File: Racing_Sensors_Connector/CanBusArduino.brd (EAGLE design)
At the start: 48.3 x 40.6 mm, 21 parts, among them U1 328P, Y1 16MHz

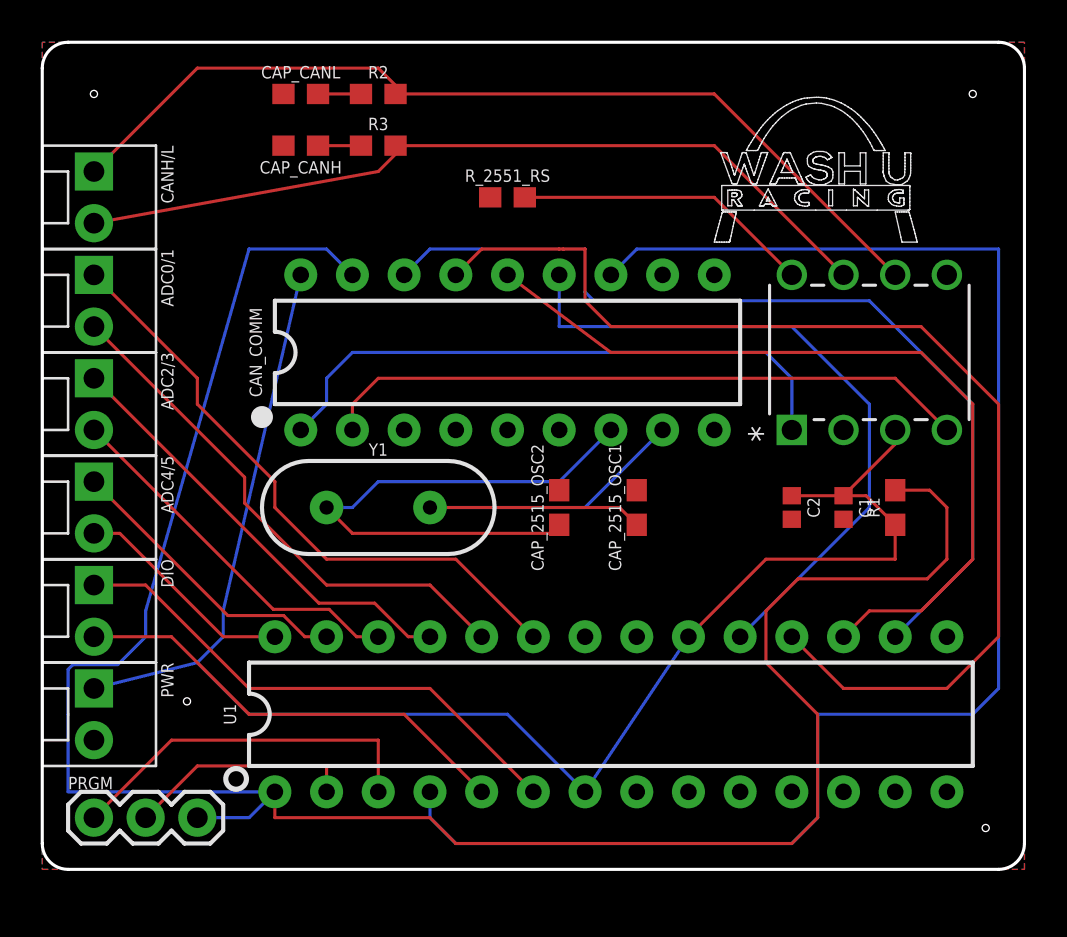
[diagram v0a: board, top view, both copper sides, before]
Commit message: Add actual mounting holes
2M clearance
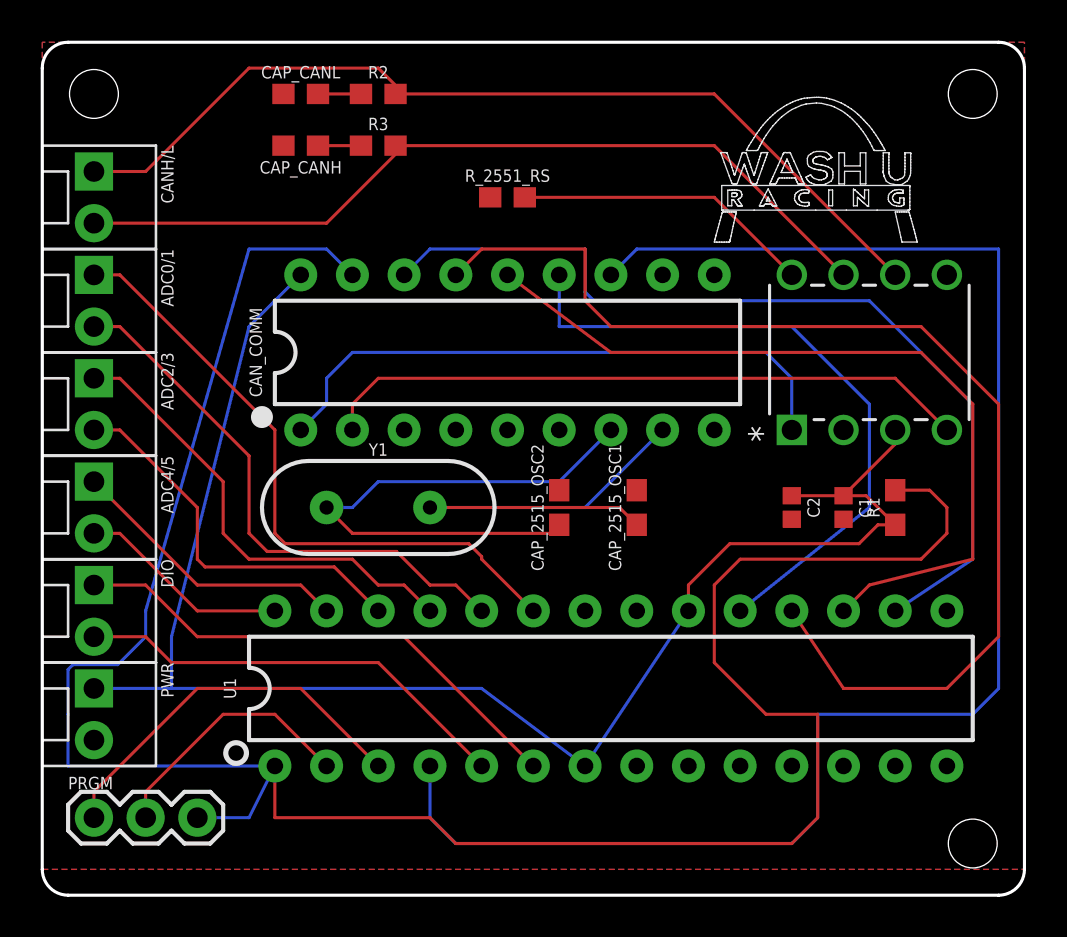
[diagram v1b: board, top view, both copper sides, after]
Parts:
- moved U1 1.27 mm to (27.9, 8.89)
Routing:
- net RS: track 105.9 -> 112.1 mm
- net RX: track 11.2 -> 12.8 mm
- net CAN_INT: track 77.0 -> 78.3 mm
- net A0: track 30.4 -> 31.5 mm
- net MISO: track 55.5 -> 56.5 mm
- net A1: track 26.1 -> 27.1 mm
- net A3: track 18.2 -> 19.1 mm
- net A2: track 21.8 -> 22.7 mm
- net MOSI: track 40.7 -> 39.8 mm
- net SCK: track 33.4 -> 32.6 mm
- net TX: track 18.1 -> 18.9 mm
- net CANH: track 40.6 -> 41.5 mm
- net CAN_CS: track 45.9 -> 45.1 mm
- net D4: track 25.8 -> 25.3 mm
- net D3: track 22.2 -> 21.7 mm
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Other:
- board size 48.3 x 40.6 mm -> 48.3 x 41.9 mm

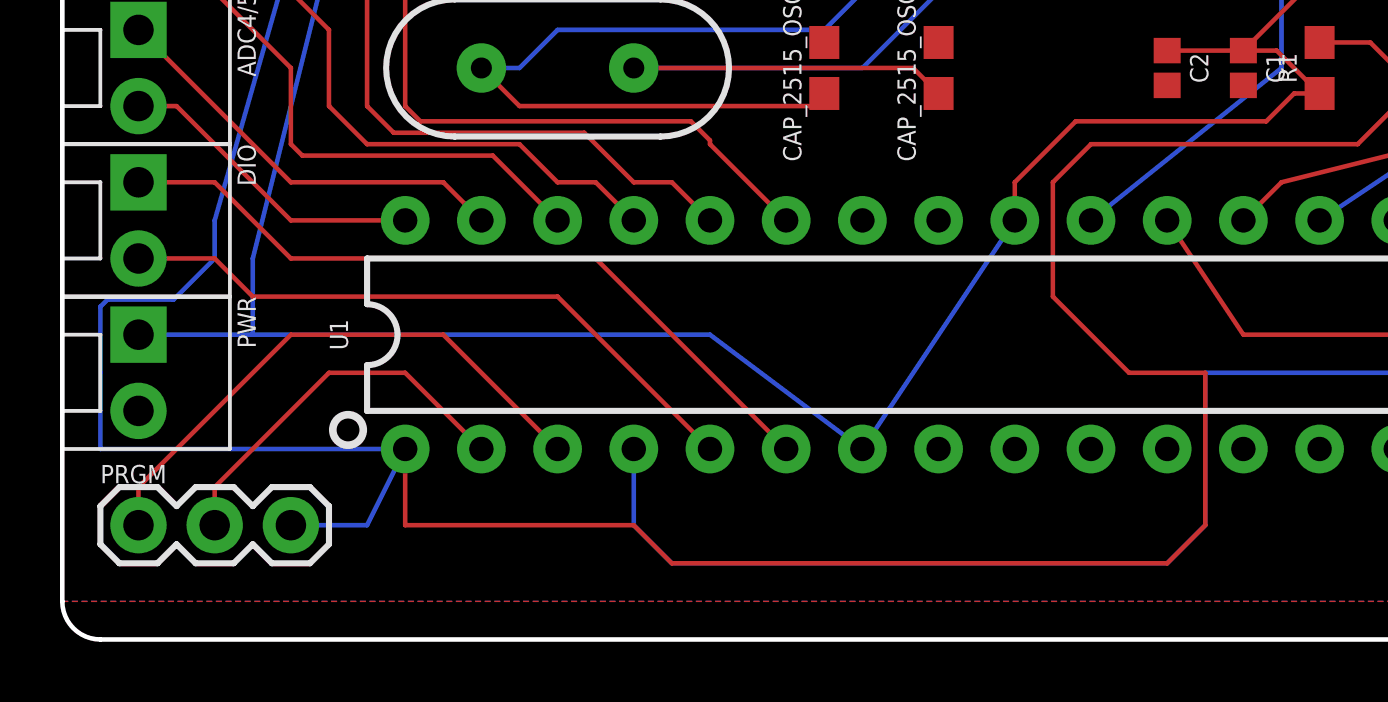
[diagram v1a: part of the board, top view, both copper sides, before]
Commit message: Move programming header to the side
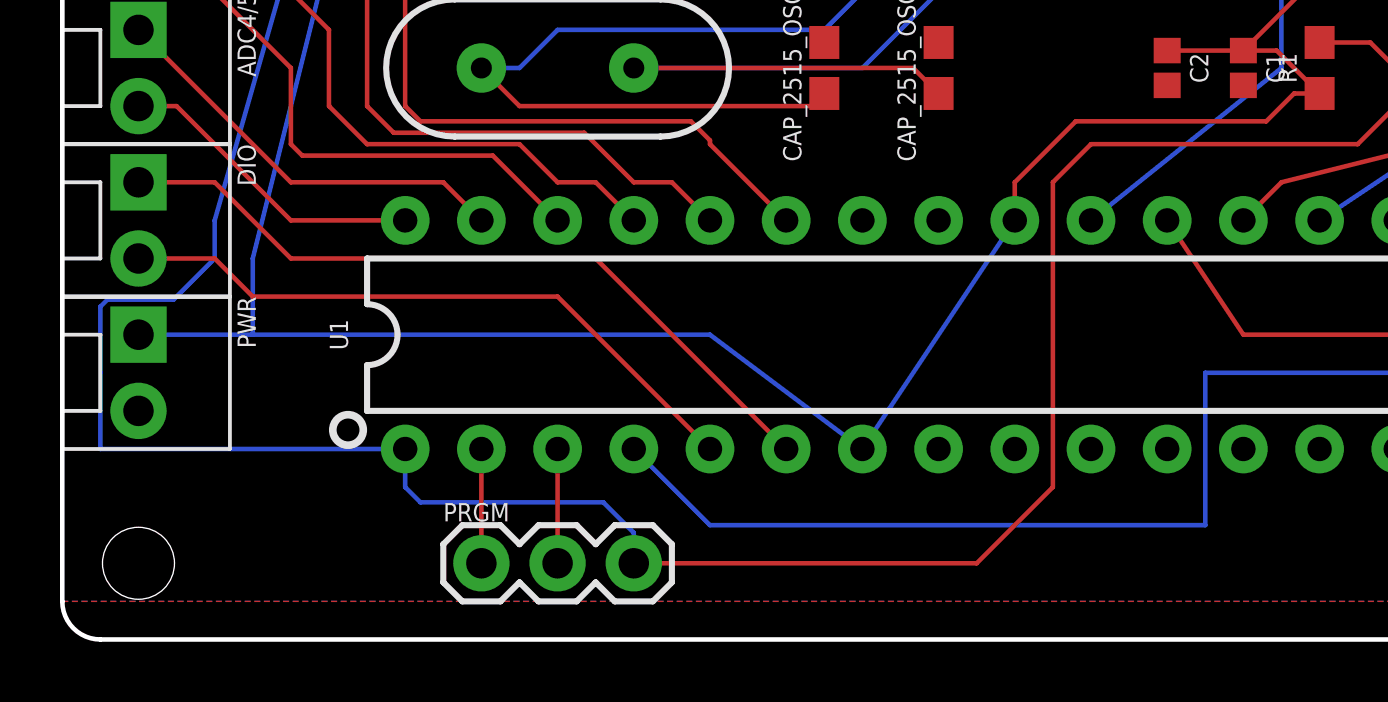
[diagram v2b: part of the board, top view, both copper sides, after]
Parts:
- moved PRGM 11.5 mm to (14.0, 1.27)
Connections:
- net RX: now also PRGM.1; no longer PRGM.2
- net TX: now also PRGM.2; no longer PRGM.1
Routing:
- net TX: track 18.9 -> 3.81 mm
- net RS: track 112.1 -> 97.1 mm
- net RX: track 12.8 -> 3.81 mm
- net CAN_INT: track 78.3 -> 75.8 mm
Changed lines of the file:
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@@
 <layer number="43" name="vRestrict" color="2" fill="10" visible="no" active="yes"/>
 <layer number="44" name="Drills" color="7" fill="1" visible="no" active="yes"/>
-<layer number="45" name="Holes" color="7" fill="1" visible="no" active="yes"/>
+<layer number="45" name="Holes" color="7" fill="1" visible="yes" active="yes"/>
 <layer number="46" name="Milling" color="3" fill="1" visible="no" active="yes"/>
 <layer number="47" name="Measures" color="7" fill="1" visible="no" active="yes"/>
@@
 <wire x1="1.27" y1="-1.27" x2="46.99" y2="-1.27" width="0.1524" layer="20"/>
 <hole x="45.72" y="1.27" drill="2.4"/>
+<hole x="2.54" y="1.27" drill="2.4"/>
 </plain>
 <attributes>
@@
 <attribute name="PROD_ID" value="CAP-12416" x="36.83" y="17.78" size="1.778" layer="27" rot="R270" display="off"/>
 </element>
-<element name="PRGM" library="SparkFun-Connectors" package="1X03" value="455-1750-1-ND" x="2.54" y="2.54">
-<attribute name="PROD_ID" value="XXX-00000" x="2.54" y="2.54" size="1.778" layer="27" display="off"/>
+<element name="PRGM" library="SparkFun-Connectors" package="1X03" value="455-1750-1-ND" x="13.97" y="1.27">
+<attribute name="PROD_ID" value="XXX-00000" x="13.97" y="1.27" size="1.778" layer="27" display="off"/>
 </element>
 <element name="PWR" library="SparkFun-Connectors" package="MOLEX-1X2" value="" x="2.54" y="8.89" rot="R270">
@@
 <contactref element="CAN_COMM" pad="12"/>
 <contactref element="U1" pad="4"/>
-<wire x1="19.05" y1="5.08" x2="19.05" y2="2.54" width="0.1524" layer="16"/>
 <wire x1="27.94" y1="29.21" x2="29.21" y2="30.48" width="0.1524" layer="16"/>
 <wire x1="46.99" y1="30.48" x2="29.21" y2="30.48" width="0.1524" layer="16"/>
-<wire x1="19.05" y1="2.54" x2="20.32" y2="1.27" width="0.1524" layer="16"/>
-<wire x1="20.32" y1="1.27" x2="36.83" y2="1.27" width="0.1524" layer="16"/>
-<wire x1="36.83" y1="1.27" x2="38.1" y2="2.54" width="0.1524" layer="16"/>
 <wire x1="38.1" y1="2.54" x2="38.1" y2="7.62" width="0.1524" layer="16"/>
 <wire x1="38.1" y1="7.62" x2="45.72" y2="7.62" width="0.1524" layer="16"/>
 <wire x1="45.72" y1="7.62" x2="46.99" y2="8.89" width="0.1524" layer="16"/>
 <wire x1="46.99" y1="8.89" x2="46.99" y2="30.48" width="0.1524" layer="16"/>
+<wire x1="19.05" y1="5.08" x2="21.59" y2="2.54" width="0.1524" layer="16"/>
+<wire x1="21.59" y1="2.54" x2="38.1" y2="2.54" width="0.1524" layer="16"/>
 </signal>
 <signal name="CAN_CS">
@@
 <contactref element="R1" pad="2"/>
 <wire x1="5.08" y1="12.7" x2="10.16" y2="30.48" width="0.1524" layer="16"/>
-<wire x1="11.43" y1="5.08" x2="11.43" y2="2.54" width="0.1524" layer="1"/>
 <wire x1="13.97" y1="30.48" x2="10.16" y2="30.48" width="0.1524" layer="16"/>
 <wire x1="13.97" y1="30.48" x2="15.24" y2="29.21" width="0.1524" layer="16"/>
 <wire x1="41.91" y1="18.63" x2="43.6" y2="18.63" width="0.1524" layer="1"/>
 <wire x1="44.45" y1="17.78" x2="43.6" y2="18.63" width="0.1524" layer="1"/>
-<wire x1="11.43" y1="2.54" x2="19.05" y2="2.54" width="0.1524" layer="1"/>
-<wire x1="19.05" y1="2.54" x2="20.32" y2="1.27" width="0.1524" layer="1"/>
 <contactref element="PRGM" pad="3"/>
 <wire x1="3.7084" y1="10.0584" x2="5.08" y2="11.43" width="0.1524" layer="16"/>
@@
 <wire x1="1.270003125" y1="9.8228875" x2="1.505515625" y2="10.0584" width="0.1524" layer="16"/>
 <wire x1="5.08" y1="11.43" x2="5.08" y2="12.7" width="0.1524" layer="16"/>
-<wire x1="7.62" y1="2.54" x2="10.16" y2="2.54" width="0.1524" layer="16"/>
-<wire x1="10.16" y1="2.54" x2="11.43" y2="5.08" width="0.1524" layer="16"/>
-<wire x1="20.32" y1="1.27" x2="36.83" y2="1.27" width="0.1524" layer="1"/>
-<wire x1="36.83" y1="1.27" x2="38.1" y2="2.54" width="0.1524" layer="1"/>
-<wire x1="38.1" y1="2.54" x2="38.1" y2="7.62" width="0.1524" layer="1"/>
 <wire x1="34.29" y1="15.24" x2="43.18" y2="15.24" width="0.1524" layer="1"/>
 <wire x1="43.18" y1="15.24" x2="44.45" y2="16.51" width="0.1524" layer="1"/>
 <wire x1="44.45" y1="16.51" x2="44.45" y2="17.78" width="0.1524" layer="1"/>
-<wire x1="1.27" y1="5.08" x2="11.43" y2="5.08" width="0.1524" layer="16"/>
+<wire x1="11.43" y1="5.08" x2="1.27" y2="5.08" width="0.1524" layer="16"/>
 <wire x1="1.27" y1="7.62" x2="1.27" y2="5.08" width="0.1524" layer="16"/>
 <wire x1="33.02" y1="13.97" x2="34.29" y2="15.24" width="0.1524" layer="1"/>
-<wire x1="38.1" y1="7.62" x2="35.56" y2="7.62" width="0.1524" layer="1"/>
-<wire x1="35.56" y1="7.62" x2="33.02" y2="10.16" width="0.1524" layer="1"/>
-<wire x1="33.02" y1="10.16" x2="33.02" y2="13.97" width="0.1524" layer="1"/>
+<wire x1="19.05" y1="1.27" x2="30.48" y2="1.27" width="0.1524" layer="1"/>
+<wire x1="30.48" y1="1.27" x2="33.02" y2="3.81" width="0.1524" layer="1"/>
+<wire x1="33.02" y1="3.81" x2="33.02" y2="13.97" width="0.1524" layer="1"/>
+<wire x1="19.05" y1="1.27" x2="19.05" y2="2.286" width="0.1524" layer="16"/>
+<wire x1="19.05" y1="2.286" x2="18.034" y2="3.302" width="0.1524" layer="16"/>
+<wire x1="18.034" y1="3.302" x2="11.938" y2="3.302" width="0.1524" layer="16"/>
+<wire x1="11.938" y1="3.302" x2="11.43" y2="3.81" width="0.1524" layer="16"/>
+<wire x1="11.43" y1="3.81" x2="11.43" y2="5.08" width="0.1524" layer="16"/>
 </signal>
 <signal name="GND">
@@
 <signal name="RX">
 <contactref element="U1" pad="2"/>
-<contactref element="PRGM" pad="2"/>
-<wire x1="13.97" y1="5.08" x2="11.43" y2="7.62" width="0.1524" layer="1"/>
-<wire x1="11.43" y1="7.62" x2="8.89" y2="7.62" width="0.1524" layer="1"/>
-<wire x1="8.89" y1="7.62" x2="5.08" y2="3.81" width="0.1524" layer="1"/>
-<wire x1="5.08" y1="3.81" x2="5.08" y2="2.54" width="0.1524" layer="1"/>
+<contactref element="PRGM" pad="1"/>
+<wire x1="13.97" y1="5.08" x2="13.97" y2="1.27" width="0.1524" layer="1"/>
 </signal>
 <signal name="TX">
 <contactref element="U1" pad="3"/>
-<contactref element="PRGM" pad="1"/>
-<wire x1="2.54" y1="2.54" x2="2.54" y2="3.81" width="0.1524" layer="1"/>
-<wire x1="2.54" y1="3.81" x2="7.62" y2="8.89" width="0.1524" layer="1"/>
-<wire x1="7.62" y1="8.89" x2="12.7" y2="8.89" width="0.1524" layer="1"/>
-<wire x1="12.7" y1="8.89" x2="16.51" y2="5.08" width="0.1524" layer="1"/>
+<contactref element="PRGM" pad="2"/>
+<wire x1="16.51" y1="5.08" x2="16.51" y2="1.27" width="0.1524" layer="1"/>
 </signal>
 <signal name="A4">

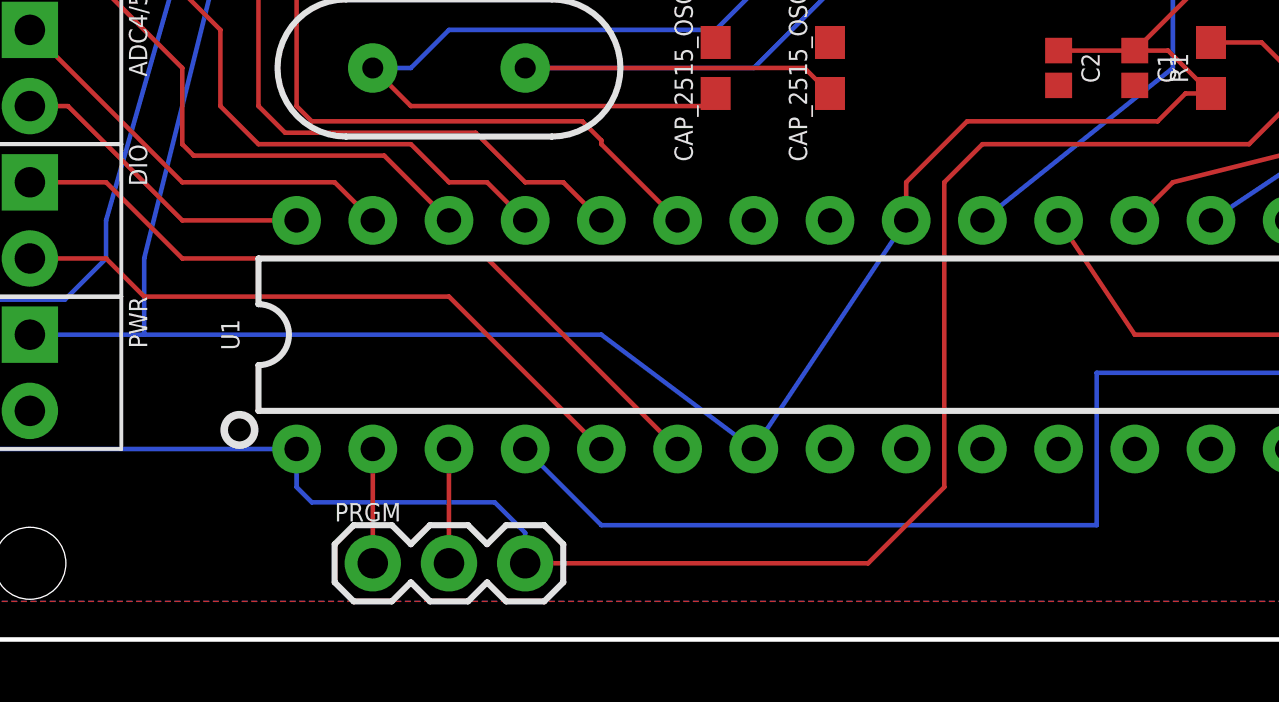
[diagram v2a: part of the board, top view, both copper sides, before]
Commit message: Move digital pin 6 to 11 (4 to 5)
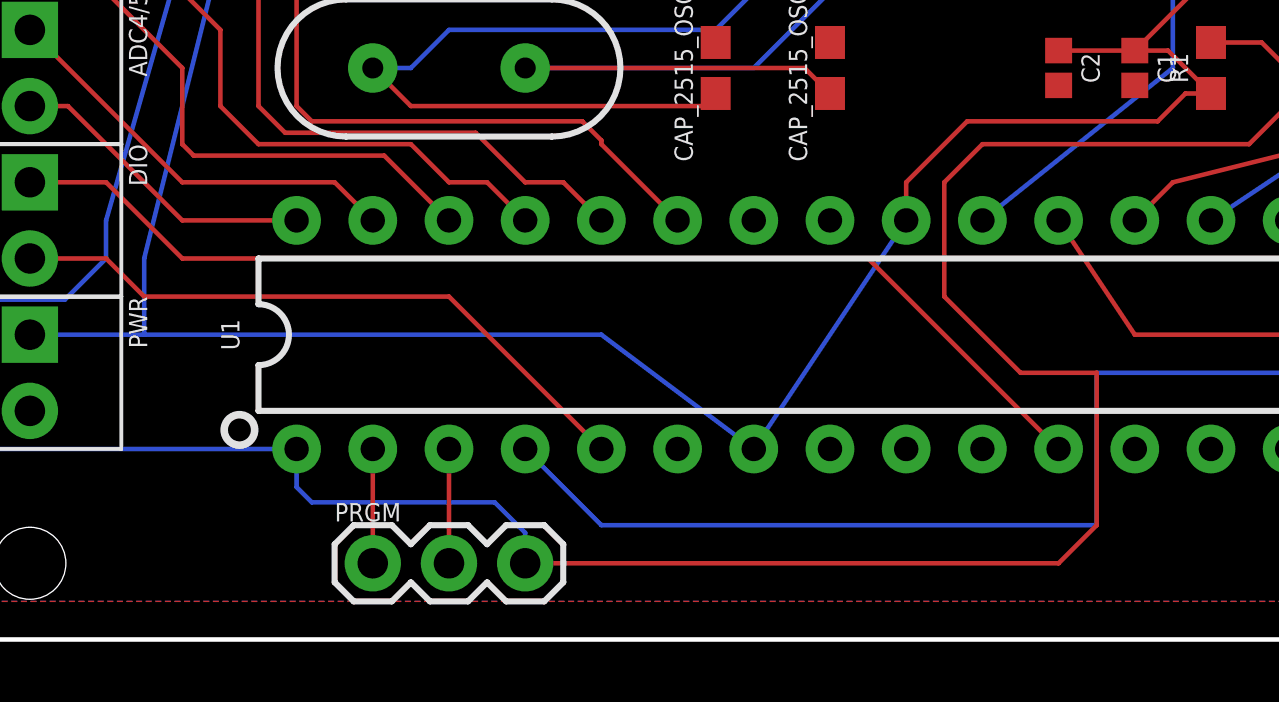
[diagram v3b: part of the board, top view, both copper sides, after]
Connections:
- net D4: now also U1.11; no longer U1.6
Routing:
- net D4: track 25.3 -> 38.0 mm
- net RS: track 97.1 -> 106.5 mm
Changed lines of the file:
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@@
 <wire x1="1.27" y1="7.62" x2="1.27" y2="5.08" width="0.1524" layer="16"/>
 <wire x1="33.02" y1="13.97" x2="34.29" y2="15.24" width="0.1524" layer="1"/>
-<wire x1="19.05" y1="1.27" x2="30.48" y2="1.27" width="0.1524" layer="1"/>
-<wire x1="30.48" y1="1.27" x2="33.02" y2="3.81" width="0.1524" layer="1"/>
-<wire x1="33.02" y1="3.81" x2="33.02" y2="13.97" width="0.1524" layer="1"/>
 <wire x1="19.05" y1="1.27" x2="19.05" y2="2.286" width="0.1524" layer="16"/>
 <wire x1="19.05" y1="2.286" x2="18.034" y2="3.302" width="0.1524" layer="16"/>
@@
 <wire x1="11.938" y1="3.302" x2="11.43" y2="3.81" width="0.1524" layer="16"/>
 <wire x1="11.43" y1="3.81" x2="11.43" y2="5.08" width="0.1524" layer="16"/>
+<wire x1="36.83" y1="1.27" x2="38.1" y2="2.54" width="0.1524" layer="1"/>
+<wire x1="38.1" y1="2.54" x2="38.1" y2="7.62" width="0.1524" layer="1"/>
+<wire x1="38.1" y1="7.62" x2="35.56" y2="7.62" width="0.1524" layer="1"/>
+<wire x1="35.56" y1="7.62" x2="33.02" y2="10.16" width="0.1524" layer="1"/>
+<wire x1="33.02" y1="10.16" x2="33.02" y2="13.97" width="0.1524" layer="1"/>
+<wire x1="19.05" y1="1.27" x2="36.83" y2="1.27" width="0.1524" layer="1"/>
 </signal>
 <signal name="GND">
@@
 </signal>
 <signal name="D4">
-<contactref element="U1" pad="6"/>
 <contactref element="DIO" pad="1"/>
 <wire x1="2.54" y1="13.97" x2="5.08" y2="13.97" width="0.1524" layer="1"/>
 <wire x1="5.08" y1="13.97" x2="7.62" y2="11.43" width="0.1524" layer="1"/>
-<wire x1="7.62" y1="11.43" x2="17.78" y2="11.43" width="0.1524" layer="1"/>
-<wire x1="17.78" y1="11.43" x2="24.13" y2="5.08" width="0.1524" layer="1"/>
+<contactref element="U1" pad="11"/>
+<wire x1="30.48" y1="11.43" x2="36.83" y2="5.08" width="0.1524" layer="1"/>
+<wire x1="7.62" y1="11.43" x2="30.48" y2="11.43" width="0.1524" layer="1"/>
 </signal>
 </signals>
